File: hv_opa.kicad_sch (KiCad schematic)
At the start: 1 part, among them IC6 PA78DK

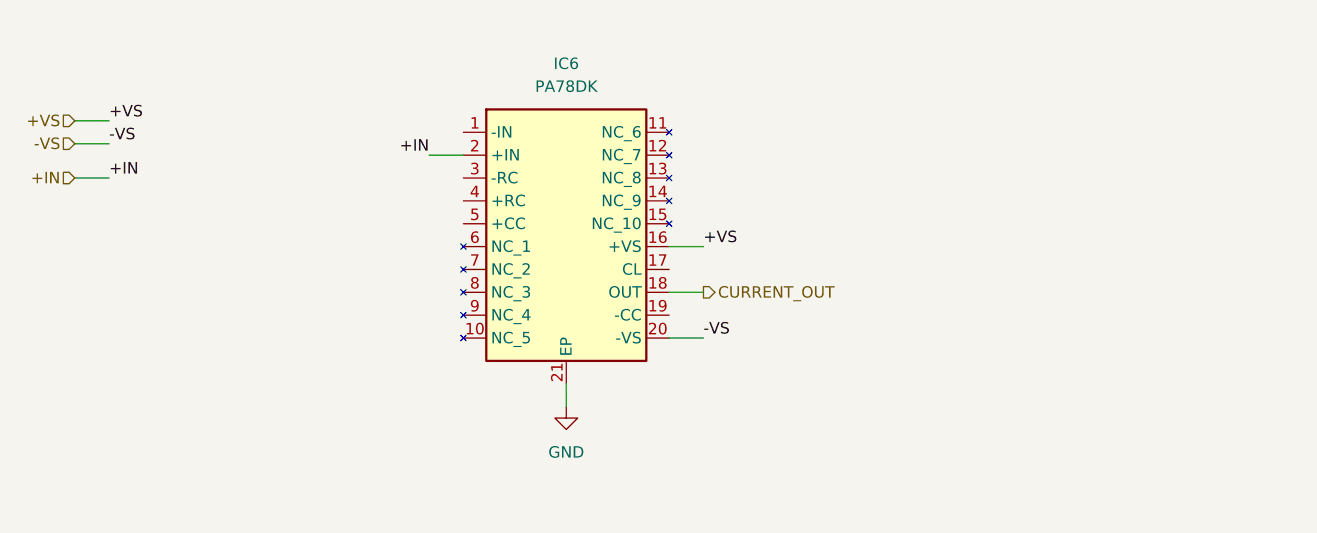
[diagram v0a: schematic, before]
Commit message: fix: resistors and capacitors values tested in LTSPICE for HV OPA page
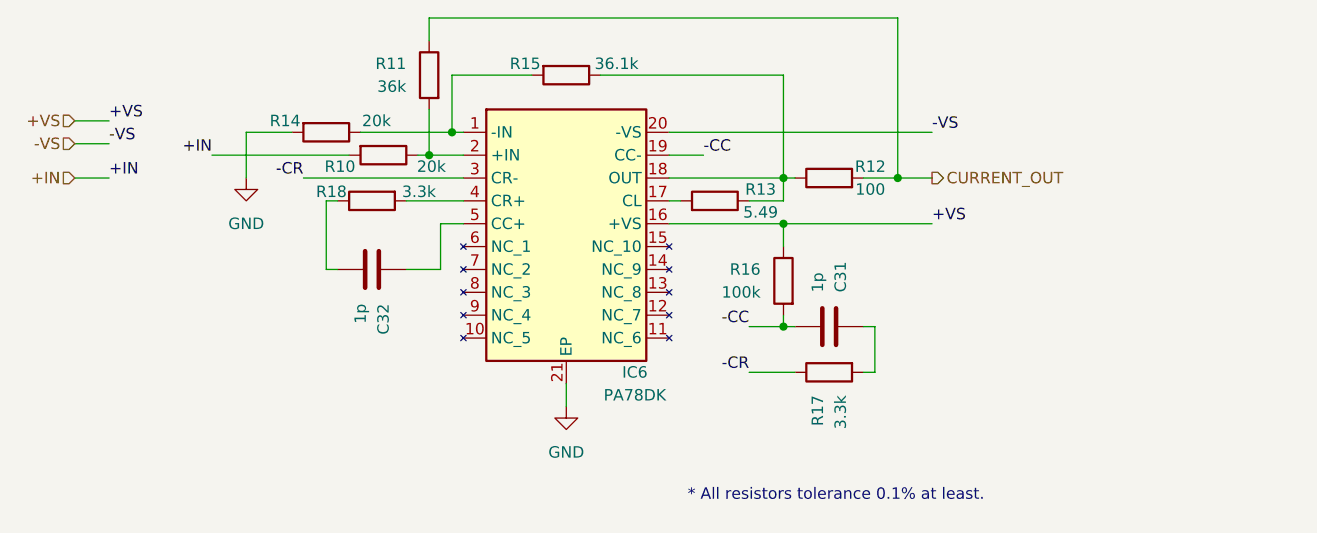
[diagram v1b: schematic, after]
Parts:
- added C31, C32: 1p, Capacitor_SMD:C_0805_2012Metric_Pad1.18x1.45mm_HandSolder, symbol Device:C
- added R10, R14: 20k, Resistor_SMD:R_0805_2012Metric_Pad1.20x1.40mm_HandSolder, symbol Device:R
- added R11: 36k, Resistor_SMD:R_0805_2012Metric_Pad1.20x1.40mm_HandSolder, symbol Device:R
- added R12: 100, Resistor_SMD:R_1206_3216Metric_Pad1.30x1.75mm_HandSolder, symbol Device:R
- added R13: 5.49, Resistor_SMD:R_0805_2012Metric_Pad1.20x1.40mm_HandSolder, symbol Device:R
- added R15: 36.1k, Resistor_SMD:R_0805_2012Metric_Pad1.20x1.40mm_HandSolder, symbol Device:R
- added R16: 100k, Resistor_SMD:R_0805_2012Metric_Pad1.20x1.40mm_HandSolder, symbol Device:R
- added R17, R18: 3.3k, Resistor_SMD:R_0805_2012Metric_Pad1.20x1.40mm_HandSolder, symbol Device:R
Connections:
- net +IN: now also R10.2; no longer IC6.2 (+IN)
- net +VS: now also R16.1
- net CURRENT_OUT: now also R11.1, R12.2; no longer IC6.18 (OUT)
- net GND: now also R14.2
- net at IC6.1 (-IN): now also R14.1, R15.2
- net at IC6.17 (CL): now also R13.2
- net -CC: now reaches IC6.19 (CC-)
- net -CC: now also C31.1, R16.2
- net -CR: now reaches IC6.3 (CR-)
- net -CR: now also R17.1
- net at IC6.4 (CR+): now also R18.2
- net at IC6.5 (CC+): now also C32.2
- new net: C31.2, R17.2
- new net: IC6.2 (+IN), R10.1, R11.2
- new net: IC6.18 (OUT), R12.1, R13.1, R15.1
- new net: C32.1, R18.1
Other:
- note added: "* All resistors tolerance 0.1% at least."

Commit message: fix: using 4.096V reference instead of 5V
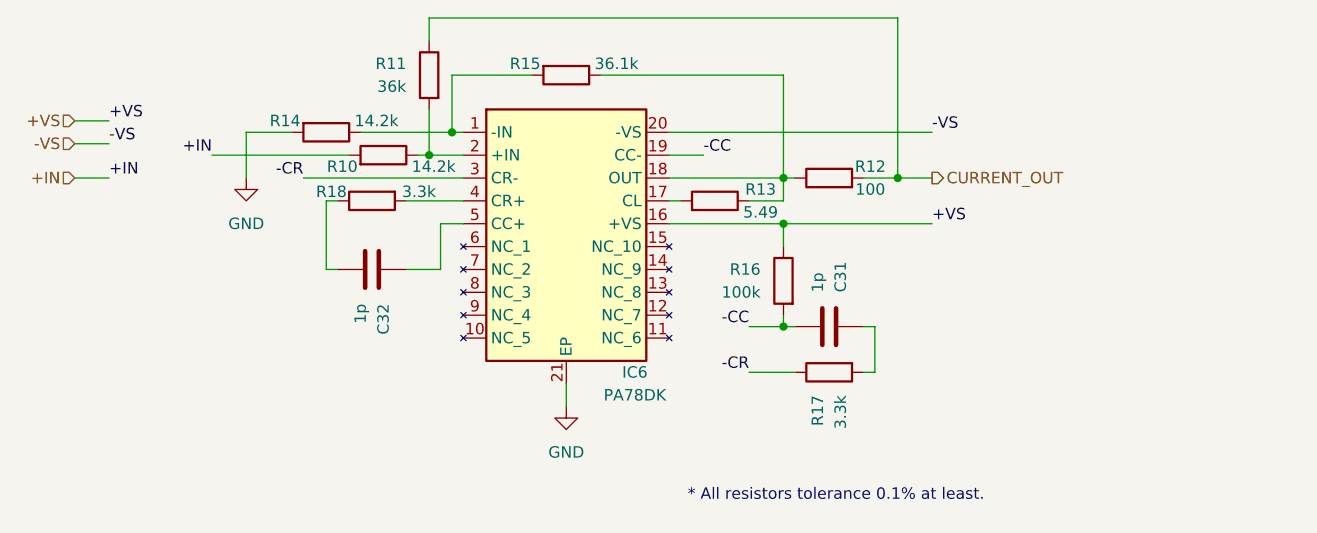
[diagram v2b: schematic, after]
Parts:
- R10, R14: value 20k -> 14.2k; MFN YAGEO -> Vishay / Dale; MFP RT0805BRD0720KL -> TNPW080514K2BEEA; S1PL https://www.mouser.dk/ProductDetail/YAGEO/RT0805BRD0720KL?q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 -> https://eu.mouser.com/ProductDetail/Vishay-Dale/TNPW080514K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
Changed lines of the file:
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@@
 			)
 		)
-		(property "Value" "20k"
+		(property "Value" "14.2k"
 			(at 127.508 66.04 90)
 			(effects
@@
 			)
 		)
-		(property "Datasheet" "https://www.mouser.dk/datasheet/2/447/PYu_RT_1_to_0_01_RoHS_L_12-3003070.pdf"
-			(at 121.92 67.31 0)
-			(effects
-				(font
-					(size 1.27 1.27)
-				)
-				(hide yes)
-			)
-		)
-		(property "Description" "Thin Film Resistors - SMD 1/8W 20K ohm .1% 25p pm"
-			(at 121.92 67.31 0)
-			(effects
-				(font
-					(size 1.27 1.27)
-				)
-				(hide yes)
-			)
-		)
-		(property "MFN" "YAGEO"
-			(at 121.92 67.31 0)
-			(effects
-				(font
-					(size 1.27 1.27)
-				)
-				(hide yes)
-			)
-		)
-		(property "MFP" "RT0805BRD0720KL"
+		(property "Datasheet" "https://www.vishay.com/doc?28758"
+			(at 121.92 67.31 0)
+			(effects
+				(font
+					(size 1.27 1.27)
+				)
+				(hide yes)
+			)
+		)
+		(property "Description" "Thin Film Resistors - SMD 1/5W 14.2K ohm .1% 25p pm"
+			(at 121.92 67.31 0)
+			(effects
+				(font
+					(size 1.27 1.27)
+				)
+				(hide yes)
+			)
+		)
+		(property "MFN" "Vishay / Dale"
+			(at 121.92 67.31 0)
+			(effects
+				(font
+					(size 1.27 1.27)
+				)
+				(hide yes)
+			)
+		)
+		(property "MFP" "TNPW080514K2BEEA"
 			(at 121.92 67.31 0)
 			(effects
@@
 			)
 		)
-		(property "S1PL" "https://www.mouser.dk/ProductDetail/YAGEO/RT0805BRD0720KL?qs=sGAEpiMZZMtlubZbdhIBINiNOdHvEUleF5hAG6YbgpQ%3D"
+		(property "S1PL" "https://eu.mouser.com/ProductDetail/Vishay-Dale/TNPW080514K2BEEA?qs=NrXEK%2Fuukt5PsC1jRy0sxw%3D%3D"
 			(at 121.92 67.31 0)
 			(effects
@@
 				(path "/1d5ae591-53a2-4652-87aa-0cddc0836341/1d3760c1-b1be-4d74-b732-ff8fe2c40888"
 					(reference "R14")
+					(unit 1)
+				)
+			)
+		)
+	)
+	(symbol
+		(lib_id "Device:R")
+		(at 128.27 69.85 270)
+		(mirror x)
+		(unit 1)
+		(exclude_from_sim no)
+		(in_bom yes)
+		(on_board yes)
+		(dnp no)
+		(property "Reference" "R10"
+			(at 123.698 71.12 90)
+			(effects
+				(font
+					(size 1.27 1.27)
+				)
+			)
+		)
+		(property "Value" "14.2k"
+			(at 133.858 71.12 90)
+			(effects
+				(font
+					(size 1.27 1.27)
+				)
+			)
+		)
+		(property "Footprint" "Resistor_SMD:R_0805_2012Metric_Pad1.20x1.40mm_HandSolder"
+			(at 128.27 71.628 90)
+			(effects
+				(font
+					(size 1.27 1.27)
+				)
+				(hide yes)
+			)
+		)
+		(property "Datasheet" "https://www.vishay.com/doc?28758"
+			(at 128.27 69.85 0)
+			(effects
+				(font
+					(size 1.27 1.27)
+				)
+				(hide yes)
+			)
+		)
+		(property "Description" "Thin Film Resistors - SMD 1/5W 14.2K ohm .1% 25p pm"
+			(at 128.27 69.85 0)
+			(effects
+				(font
+					(size 1.27 1.27)
+				)
+				(hide yes)
+			)
+		)
+		(property "MFN" "Vishay / Dale"
+			(at 128.27 69.85 0)
+			(effects
+				(font
+					(size 1.27 1.27)
+				)
+				(hide yes)
+			)
+		)
+		(property "MFP" "TNPW080514K2BEEA"
+			(at 128.27 69.85 0)
+			(effects
+				(font
+					(size 1.27 1.27)
+				)
+				(hide yes)
+			)
+		)
+		(property "S1PN" "Mouser"
+			(at 128.27 69.85 0)
+			(effects
+				(font
+					(size 1.27 1.27)
+				)
+				(hide yes)
+			)
+		)
+		(property "S1PL" "https://eu.mouser.com/ProductDetail/Vishay-Dale/TNPW080514K2BEEA?qs=NrXEK%2Fuukt5PsC1jRy0sxw%3D%3D"
+			(at 128.27 69.85 0)
+			(effects
+				(font
+					(size 1.27 1.27)
+				)
+				(hide yes)
+			)
+		)
+		(pin "1"
+		)
+		(pin "2"
+		)
+		(instances
+			(project "techstim-hardware"
+				(path "/1d5ae591-53a2-4652-87aa-0cddc0836341/1d3760c1-b1be-4d74-b732-ff8fe2c40888"
+					(reference "R10")
 					(unit 1)
 				)
@@
 					(unit 1)
 				)
-			)
-		)
-	)
-	(symbol
-		(lib_id "Device:R")
-		(at 128.27 69.85 270)
-		(unit 1)
-		(exclude_from_sim no)
-		(in_bom yes)
-		(on_board yes)
-		(dnp no)
-		(property "Reference" "R10"
-			(at 123.444 71.12 90)
-			(effects
-				(font
-					(size 1.27 1.27)
-				)
-			)
-		)
-		(property "Value" "20k"
-			(at 133.604 71.12 90)
-			(effects
-				(font
-					(size 1.27 1.27)
-				)
-			)
-		)
-		(property "Footprint" "Resistor_SMD:R_0805_2012Metric_Pad1.20x1.40mm_HandSolder"
-			(at 128.27 68.072 90)
-			(effects
-				(font
-					(size 1.27 1.27)
-				)
-				(hide yes)
-			)
-		)
-		(property "Datasheet" "https://www.mouser.dk/datasheet/2/447/PYu_RT_1_to_0_01_RoHS_L_12-3003070.pdf"
-			(at 128.27 69.85 0)
-			(effects
-				(font
-					(size 1.27 1.27)
-				)
-				(hide yes)
-			)
-		)
-		(property "Description" "Thin Film Resistors - SMD 1/8W 20K ohm .1% 25p pm"
-			(at 128.27 69.85 0)
-			(effects
-				(font
-					(size 1.27 1.27)
-				)
-				(hide yes)
-			)
-		)
-		(property "MFN" "YAGEO"
-			(at 128.27 69.85 0)
-			(effects
-				(font
-					(size 1.27 1.27)
-				)
-				(hide yes)
-			)
-		)
-		(property "MFP" "RT0805BRD0720KL"
-			(at 128.27 69.85 0)
-			(effects
-				(font
-					(size 1.27 1.27)
-				)
-				(hide yes)
-			)
-		)
-		(property "S1PN" "Mouser"
-			(at 128.27 69.85 0)
-			(effects
-				(font
-					(size 1.27 1.27)
-				)
-				(hide yes)
-			)
-		)
-		(property "S1PL" "https://www.mouser.dk/ProductDetail/YAGEO/RT0805BRD0720KL?qs=sGAEpiMZZMtlubZbdhIBINiNOdHvEUleF5hAG6YbgpQ%3D"
-			(at 128.27 69.85 0)
-			(effects
-				(font
-					(size 1.27 1.27)
-				)
-				(hide yes)
-			)
-		)
-		(pin "1"
-		)
-		(pin "2"
-		)
-		(instances
-			(project "techstim-hardware"
-				(path "/1d5ae591-53a2-4652-87aa-0cddc0836341/1d3760c1-b1be-4d74-b732-ff8fe2c40888"
-					(reference "R10")
-					(unit 1)
-				)

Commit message: refactor: adding info for tolerance in capacitors for HVOPA
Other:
- note added: "* All resistors tolerance are 0.1% or less. * Capactiros are NP0."
- note removed: "* All resistors tolerance 0.1% at least."
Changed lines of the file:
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@@
 		)
 	)
-	(text "* All resistors tolerance 0.1% at least."
+	(text "* All resistors tolerance are 0.1% or less.\n* Capactiros are NP0."
 		(exclude_from_sim no)
 		(at 178.562 107.696 0)
@@
 				(size 1.27 1.27)
 			)
+			(justify left)
 		)
 	)

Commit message: fix: update PCB with last 3dmodels and ICs (ISO7640, GNDISO)
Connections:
- net GND renamed GNDISO
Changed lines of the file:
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@@
-	(wire
-		(pts
-			(xy 148.59 95.25) (xy 148.59 97.79)
-		)
-		(stroke
-			(width 0)
-			(type default)
-		)
-	)
 	(wire
 		(pts
@@
 		(pts
 			(xy 168.91 88.9) (xy 172.72 88.9)
+		)
+		(stroke
+			(width 0)
+			(type default)
+		)
+	)
+	(wire
+		(pts
+			(xy 148.59 95.25) (xy 148.59 99.06)
 		)
 		(stroke
@@
 	)
 	(symbol
-		(lib_id "power:GND")
-		(at 148.59 97.79 0)
-		(unit 1)
-		(exclude_from_sim no)
-		(in_bom yes)
-		(on_board yes)
-		(dnp no)
-		(fields_autoplaced yes)
-		(property "Reference" "#PWR077"
-			(at 148.59 104.14 0)
-			(effects
-				(font
-					(size 1.27 1.27)
-				)
-				(hide yes)
-			)
-		)
-		(property "Value" "GND"
-			(at 148.59 102.87 0)
-			(effects
-				(font
-					(size 1.27 1.27)
-				)
-			)
-		)
-		(property "Footprint" ""
-			(at 148.59 97.79 0)
-			(effects
-				(font
-					(size 1.27 1.27)
-				)
-				(hide yes)
-			)
-		)
-		(property "Datasheet" ""
-			(at 148.59 97.79 0)
-			(effects
-				(font
-					(size 1.27 1.27)
-				)
-				(hide yes)
-			)
-		)
-		(property "Description" "Power symbol creates a global label with name \"GND\" , ground"
-			(at 148.59 97.79 0)
-			(effects
-				(font
-					(size 1.27 1.27)
-				)
-				(hide yes)
-			)
-		)
-		(pin "1"
-		)
-		(instances
-			(project "techstim-hardware"
-				(path "/1d5ae591-53a2-4652-87aa-0cddc0836341/1d3760c1-b1be-4d74-b732-ff8fe2c40888"
-					(reference "#PWR077")
-					(unit 1)
-				)
-			)
-		)
-	)
-	(symbol
 		(lib_id "Device:R")
 		(at 133.35 60.96 0)
@@
 				(path "/1d5ae591-53a2-4652-87aa-0cddc0836341/1d3760c1-b1be-4d74-b732-ff8fe2c40888"
 					(reference "R11")
+					(unit 1)
+				)
+			)
+		)
+	)
+	(symbol
+		(lib_id "power:GND3")
+		(at 148.59 99.06 0)
+		(unit 1)
+		(exclude_from_sim no)
+		(in_bom yes)
+		(on_board yes)
+		(dnp no)
+		(fields_autoplaced yes)
+		(property "Reference" "#PWR035"
+			(at 148.59 105.41 0)
+			(effects
+				(font
+					(size 1.27 1.27)
+				)
+				(hide yes)
+			)
+		)
+		(property "Value" "GNDISO"
+			(at 148.59 104.14 0)
+			(effects
+				(font
+					(size 1.27 1.27)
+				)
+			)
+		)
+		(property "Footprint" ""
+			(at 148.59 99.06 0)
+			(effects
+				(font
+					(size 1.27 1.27)
+				)
+				(hide yes)
+			)
+		)
+		(property "Datasheet" ""
+			(at 148.59 99.06 0)
+			(effects
+				(font
+					(size 1.27 1.27)
+				)
+				(hide yes)
+			)
+		)
+		(property "Description" "Power symbol creates a global label with name \"GND3\" , ground"
+			(at 148.59 99.06 0)
+			(effects
+				(font
+					(size 1.27 1.27)
+				)
+				(hide yes)
+			)
+		)
+		(pin "1"
+		)
+		(instances
+			(project "techstim-hardware"
+				(path "/1d5ae591-53a2-4652-87aa-0cddc0836341/1d3760c1-b1be-4d74-b732-ff8fe2c40888"
+					(reference "#PWR035")
 					(unit 1)
 				)
@@
 	)
 	(symbol
+		(lib_id "power:GND3")
+		(at 113.03 72.39 0)
+		(unit 1)
+		(exclude_from_sim no)
+		(in_bom yes)
+		(on_board yes)
+		(dnp no)
+		(fields_autoplaced yes)
+		(property "Reference" "#PWR036"
+			(at 113.03 78.74 0)
+			(effects
+				(font
+					(size 1.27 1.27)
+				)
+				(hide yes)
+			)
+		)
+		(property "Value" "GNDISO"
+			(at 113.03 77.47 0)
+			(effects
+				(font
+					(size 1.27 1.27)
+				)
+			)
+		)
+		(property "Footprint" ""
+			(at 113.03 72.39 0)
+			(effects
+				(font
+					(size 1.27 1.27)
+				)
+				(hide yes)
+			)
+		)
+		(property "Datasheet" ""
+			(at 113.03 72.39 0)
+			(effects
+				(font
+					(size 1.27 1.27)
+				)
+				(hide yes)
+			)
+		)
+		(property "Description" "Power symbol creates a global label with name \"GND3\" , ground"
+			(at 113.03 72.39 0)
+			(effects
+				(font
+					(size 1.27 1.27)
+				)
+				(hide yes)
+			)
+		)
+		(pin "1"
+		)
+		(instances
+			(project "techstim-hardware"
+				(path "/1d5ae591-53a2-4652-87aa-0cddc0836341/1d3760c1-b1be-4d74-b732-ff8fe2c40888"
+					(reference "#PWR036")
+					(unit 1)
+				)
+			)
+		)
+	)
+	(symbol
 		(lib_id "Device:R")
 		(at 172.72 83.82 0)
@@
 					(unit 1)
 				)
-			)
-		)
-	)
-	(symbol
-		(lib_id "power:GND")
-		(at 113.03 72.39 0)
-		(unit 1)
-		(exclude_from_sim no)
-		(in_bom yes)
-		(on_board yes)
-		(dnp no)
-		(fields_autoplaced yes)
-		(property "Reference" "#PWR078"
-			(at 113.03 78.74 0)
-			(effects
-				(font
-					(size 1.27 1.27)
-				)
-				(hide yes)
-			)
-		)
-		(property "Value" "GND"
-			(at 113.03 77.47 0)
-			(effects
-				(font
-					(size 1.27 1.27)
-				)
-			)
-		)
-		(property "Footprint" ""
-			(at 113.03 72.39 0)
-			(effects
-				(font
-					(size 1.27 1.27)
-				)
-				(hide yes)
-			)
-		)
-		(property "Datasheet" ""
-			(at 113.03 72.39 0)
-			(effects
-				(font
-					(size 1.27 1.27)
-				)
-				(hide yes)
-			)
-		)
-		(property "Description" "Power symbol creates a global label with name \"GND\" , ground"
-			(at 113.03 72.39 0)
-			(effects
-				(font
-					(size 1.27 1.27)
-				)
-				(hide yes)
-			)
-		)
-		(pin "1"
-		)
-		(instances
-			(project "techstim-hardware"
-				(path "/1d5ae591-53a2-4652-87aa-0cddc0836341/1d3760c1-b1be-4d74-b732-ff8fe2c40888"
-					(reference "#PWR078")
-					(unit 1)
-				)

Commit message: fix: update Rcl with stock in supplier
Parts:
- R13: MFP CPF0805B5R49E1 -> RN73C2A6R04BTDF; S1PL https://www.mouser.dk/ProductDetail/TE-Connectivity-Holswor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 -> https://eu.mouser.com/ProductDetail/TE-Connectivity-Holswor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
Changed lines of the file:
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@@
 			)
 		)
-		(property "Description" "Thin Film Resistors - SMD CPF 0805 5R49 0.1% 25PPM"
+		(property "Description" "Thin Film Resistors - SMD RN 0805 6R04 0.1% 10PPM"
 			(at 165.1 74.93 0)
 			(effects
@@
 			)
 		)
-		(property "MFP" "CPF0805B5R49E1"
+		(property "MFP" "RN73C2A6R04BTDF"
 			(at 165.1 74.93 0)
 			(effects
@@
 			)
 		)
-		(property "S1PL" "https://www.mouser.dk/ProductDetail/TE-Connectivity-Holsworthy/CPF0805B5R49E1?qs=Im7Ui%252B8riBV4Yph%2FRlN8Tg%3D%3D"
+		(property "S1PL" "https://eu.mouser.com/ProductDetail/TE-Connectivity-Holsworthy/RN73C2A6R04BTDF?qs=9ylKvqdyudnctbznyeQKNw%3D%3D"
 			(at 165.1 74.93 0)
 			(effects

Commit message: ops: adding SP1# field and add all the info for each component
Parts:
- C31, C32: S1P# (none) -> 710-885012007094
- IC6: S1P# (none) -> 137-PA78DK; S1PN (none) -> Mouser
- R10, R14: S1P# (none) -> 71-TNPW080514K2BEEA
- R11: S1P# (none) -> 667-ERA-6AEB363V
- R12: S1P# (none) -> 71-PCAN1206E1000BST5
- R13: value 5.49 -> 6.04; S1P# (none) -> 279-RN73C2A6R04BTDF
- R15: S1P# (none) -> 71-TNPW080536K1BETY
- R16: S1P# (none) -> 71-TNPW0805100KBEEA
- R17, R18: S1P# (none) -> 667-ERA-6AEB332V
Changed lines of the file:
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@@
+			)
+		)
+		(property "S1P#" "667-ERA-6AEB332V"
+			(at 177.8 93.98 0)
+			(effects
+				(font
+					(size 1.27 1.27)
+				)
+				(hide yes)
 			)
 		)
@@
 			)
 		)
+		(property "S1P#" "710-885012007094 "
+			(at 177.8 88.9 0)
+			(effects
+				(font
+					(size 1.27 1.27)
+				)
+				(hide yes)
+			)
+		)
 		(pin "1"
 		)
@@
 			)
 		)
+		(property "S1P#" "667-ERA-6AEB363V"
+			(at 133.35 60.96 0)
+			(effects
+				(font
+					(size 1.27 1.27)
+				)
+				(hide yes)
+			)
+		)
 		(pin "1"
 		)
@@
 			)
 		)
-		(property "S1PN" ""
+		(property "S1PN" "Mouser"
 			(at 137.16 67.31 0)
 			(effects
@@
 		)
 		(property "S1PL" "https://www.mouser.co.uk/ProductDetail/Apex-Microtechnology/PA78DK?qs=TiOZkKH1s2QqTC8ILc9obg%3D%3D"
+			(at 137.16 67.31 0)
+			(effects
+				(font
+					(size 1.27 1.27)
+				)
+				(hide yes)
+			)
+		)
+		(property "S1P#" "137-PA78DK"
 			(at 137.16 67.31 0)
 			(effects
@@
 		)
 		(property "S1PL" "https://eu.mouser.com/ProductDetail/Vishay-Dale/TNPW080514K2BEEA?qs=NrXEK%2Fuukt5PsC1jRy0sxw%3D%3D"
+			(at 121.92 67.31 0)
+			(effects
+				(font
+					(size 1.27 1.27)
+				)
+				(hide yes)
+			)
+		)
+		(property "S1P#" "71-TNPW080514K2BEEA"
 			(at 121.92 67.31 0)
 			(effects
@@
 			)
 		)
+		(property "S1P#" "71-TNPW080514K2BEEA"
+			(at 128.27 69.85 0)
+			(effects
+				(font
+					(size 1.27 1.27)
+				)
+				(hide yes)
+			)
+		)
 		(pin "1"
 		)
@@
 		)
 		(property "S1PL" "https://www.mouser.dk/ProductDetail/Wurth-Elektronik/885012007094?qs=sGAEpiMZZMsh%252B1woXyUXj88C7E9rEmUTF2BIos9tuFA%3D"
+			(at 127 82.55 0)
+			(effects
+				(font
+					(size 1.27 1.27)
+				)
+				(hide yes)
+			)
+		)
+		(property "S1P#" "710-885012007094 "
 			(at 127 82.55 0)
 			(effects
@@
 			)
 		)
+		(property "S1P#" "71-TNPW0805100KBEEA"
+			(at 172.72 83.82 0)
+			(effects
+				(font
+					(size 1.27 1.27)
+				)
+				(hide yes)
+			)
+		)
 		(pin "1"
 		)
@@
 		)
 		(property "S1PL" "https://www.mouser.dk/ProductDetail/Vishay-Dale/TNPW080536K1BETY?qs=mNg%252BuB3fXm9WM1dNE9VmcA%3D%3D"
+			(at 148.59 60.96 0)
+			(effects
+				(font
+					(size 1.27 1.27)
+				)
+				(hide yes)
+			)
+		)
+		(property "S1P#" "71-TNPW080536K1BETY"
 			(at 148.59 60.96 0)
 			(effects
@@
 			)
 		)
+		(property "S1P#" "667-ERA-6AEB332V"
+			(at 127 74.93 0)
+			(effects
+				(font
+					(size 1.27 1.27)
+				)
+				(hide yes)
+			)
+		)
 		(pin "1"
 		)
@@
 		)
 		(property "S1PL" "https://www.mouser.dk/ProductDetail/Vishay-Thin-Film/PCAN1206E1000BST5?qs=sGAEpiMZZMtlubZbdhIBIPDLwbSE2XJWf%252BNJQNn%2Fc2w%3D"
+			(at 177.8 72.39 0)
+			(effects
+				(font
+					(size 1.27 1.27)
+				)
+				(hide yes)
+			)
+		)
+		(property "S1P#" "71-PCAN1206E1000BST5"
 			(at 177.8 72.39 0)
 			(effects
@@
 			)
 		)
-		(property "Value" "5.49"
+		(property "Value" "6.04"
 			(at 170.18 76.2 90)
 			(effects
@@
 			(at 165.1 74.93 0)
 			(effects
+				(font
+					(size 1.27 1.27)
+				)
+				(hide yes)
+			)
+		)
+		(property "S1P#" "279-RN73C2A6R04BTDF"
+			(at 165.1 74.93 0)
+			(effects

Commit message: fix: update names for IC components
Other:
- note added: "* All resistors tolerance are 0.1% or less. * Capacitos are NP0."
- note removed: "* All resistors tolerance are 0.1% or less. * Capactiros are NP0."
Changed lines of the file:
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@@
 		)
 	)
-	(text "* All resistors tolerance are 0.1% or less.\n* Capactiros are NP0."
+	(text "* All resistors tolerance are 0.1% or less.\n* Capacitos are NP0."
 		(exclude_from_sim no)
 		(at 178.562 107.696 0)
